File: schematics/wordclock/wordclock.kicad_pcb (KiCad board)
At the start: 2 copper layers, 66 parts, among them U1 STM32F303RCTx, U2 MAX7219

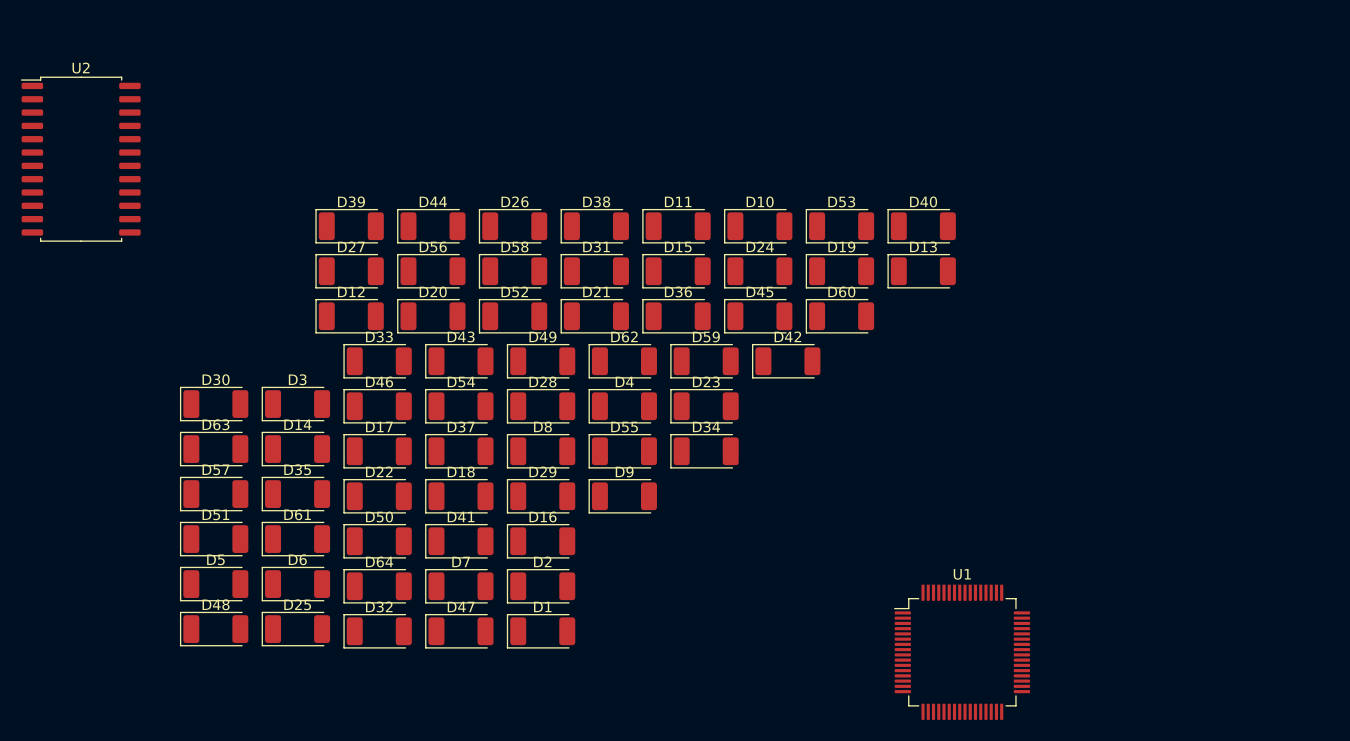
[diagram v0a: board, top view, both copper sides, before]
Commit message: Finish defining words, schematic updates
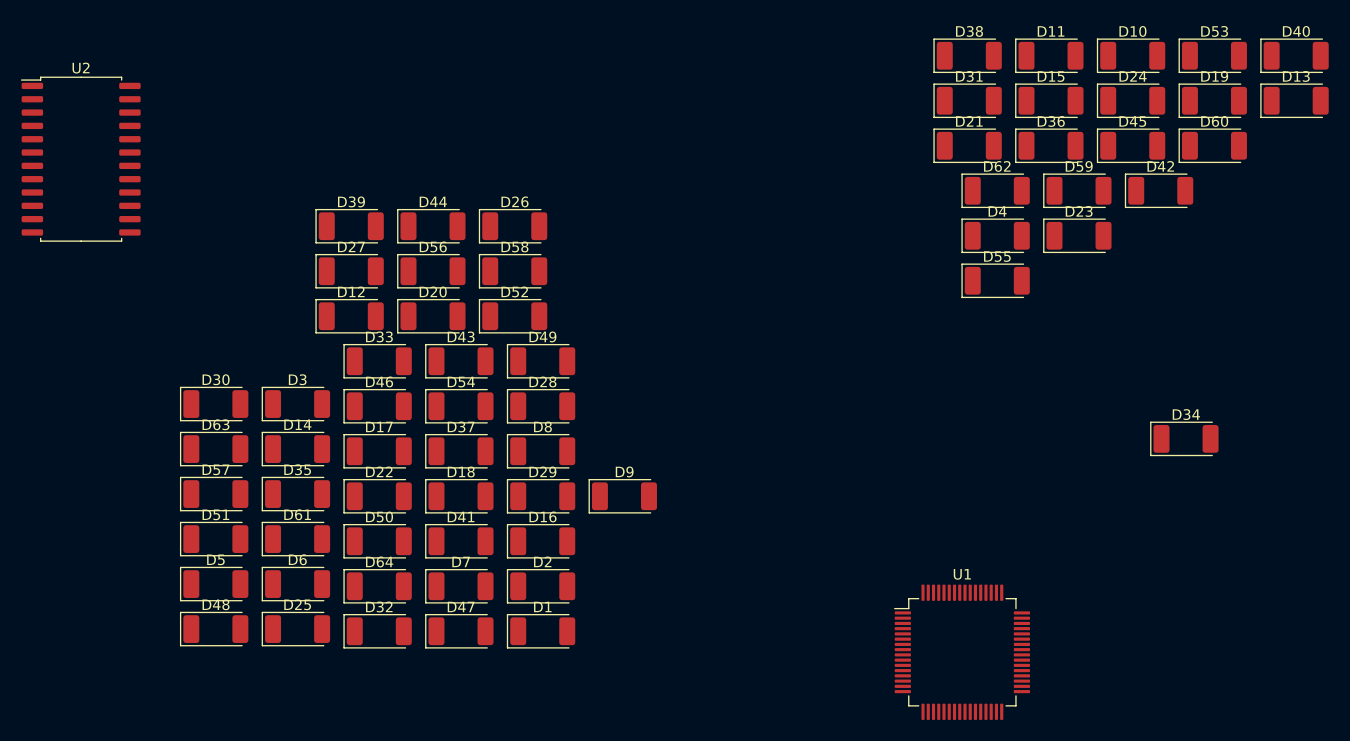
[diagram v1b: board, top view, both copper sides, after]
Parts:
- moved D34 45.8 mm to (147.3, 73.7)
- moved D10 39.1 mm to (142.2, 37.1)
- moved D19 39.1 mm to (150.0, 41.4)
- moved D23 39.1 mm to (137.1, 54.3)
- moved D24 39.1 mm to (142.2, 41.4)
- moved D4 39.1 mm to (129.3, 54.3)
- moved D45 39.1 mm to (142.2, 45.7)
- moved D53 39.1 mm to (150.0, 37.1)
- moved D55 39.1 mm to (129.3, 58.6)
- moved D59 39.1 mm to (137.1, 50.0)
- moved D60 39.1 mm to (150.0, 45.7)
- moved D62 39.1 mm to (129.3, 50.0)
- moved D42 39.1 mm to (144.9, 50.0)
- moved D11 39.1 mm to (134.4, 37.1)
- moved D13 39.1 mm to (157.8, 41.4)
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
